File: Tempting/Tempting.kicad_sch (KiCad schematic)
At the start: 10 parts, among them U101 STM32WB55CGUx, U102 SCD41-D-R2

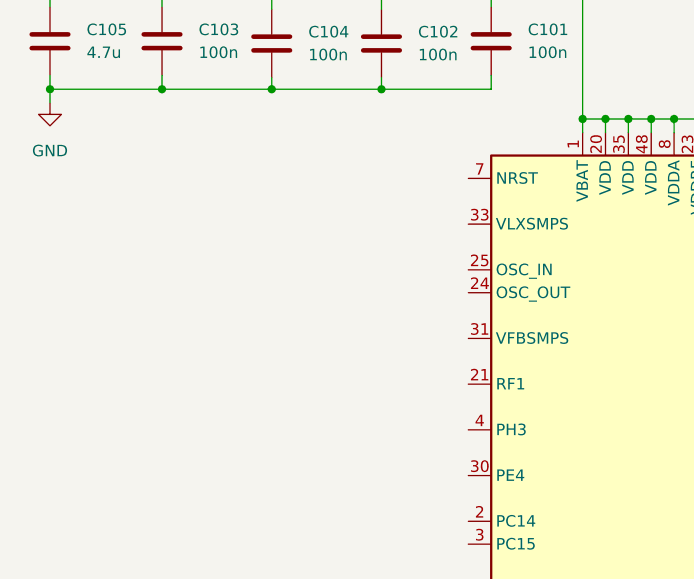
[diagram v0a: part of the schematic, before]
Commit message: Added crystals
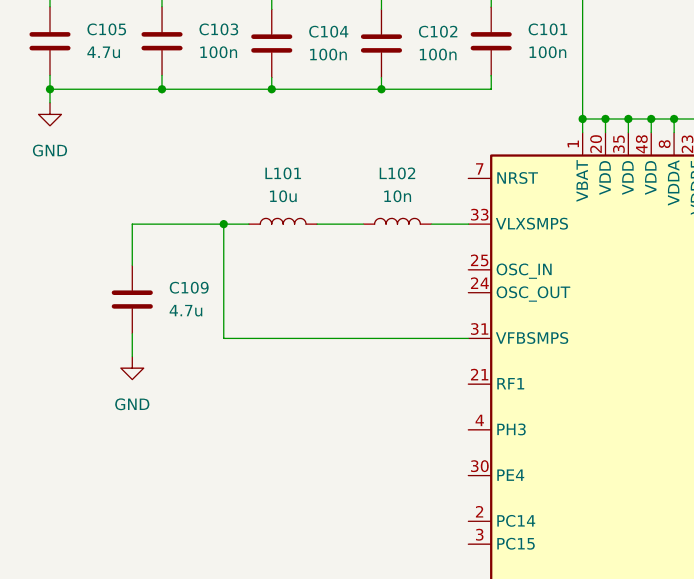
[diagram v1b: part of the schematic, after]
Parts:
- added C109: 4.7u, symbol Device:C
- added L101: 10u, symbol Device:L
- added L102: 10n, symbol Device:L
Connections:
- net GND: now also C109.2
- net at U101.31 (VFBSMPS): now also C109.1, L101.1
- net at U101.33 (VLXSMPS): now also L102.2
- new net: L101.2, L102.1

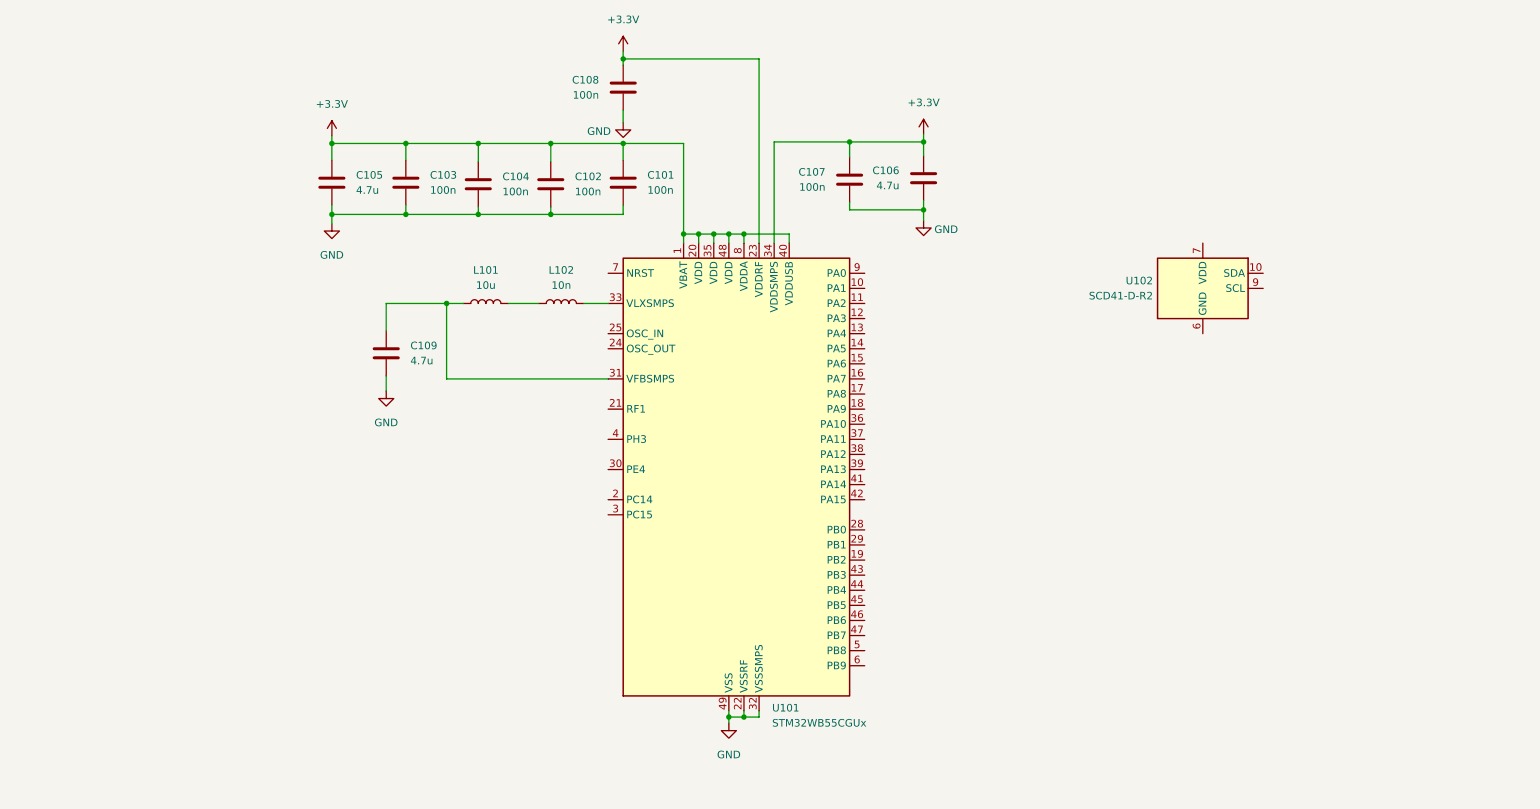
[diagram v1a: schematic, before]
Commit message: Added RF circuitry to schematic
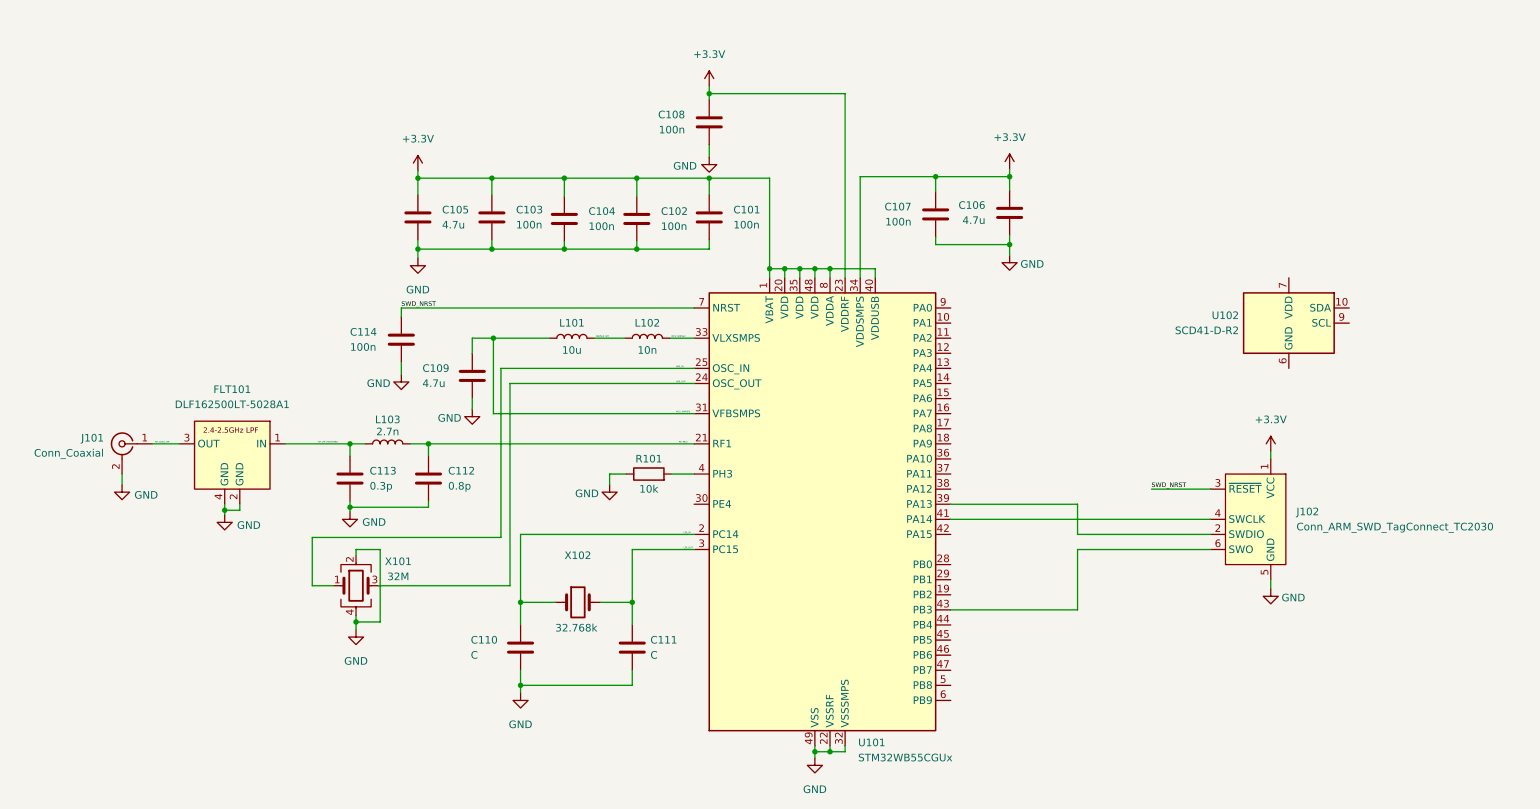
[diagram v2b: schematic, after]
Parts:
- added C110, C111: C, symbol Device:C
- added C112: 0.8p, symbol Device:C
- added C113: 0.3p, symbol Device:C
- added C114: 100n, symbol Device:C
- added FLT101: DLF162500LT-5028A1, Tempting_Footprint_Libraries:DLF162500LT-5028A1, symbol Tempting_Symbol_Libraries:DLF162500LT-5028A1
- added J101: Conn_Coaxial, symbol Connector:Conn_Coaxial
- added J102: Conn_ARM_SWD_TagConnect_TC2030, Connector:Tag-Connect_TC2030-IDC-FP_2x03_P1.27mm_Vertical, symbol Connector:Conn_ARM_SWD_TagConnect_TC2030
- added L103: 2.7n, symbol Device:L
- added R101: 10k, symbol Device:R
- added X101: 32M, symbol Device:Crystal_GND24
- added X102: 32.768k, symbol Device:Crystal
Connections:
- net +3.3V: now also J102.1 (VCC)
- net GND: now also C110.2, C111.2, C112.2, C113.2, C114.2, FLT101.2 (GND), FLT101.4 (GND), J101.2 (Ext), J102.5 (GND), R101.1, X101.2, X101.4
- net MCU_SMPSFB: now reaches C109.1, L101.1, U101.31 (VFBSMPS)
- net LSE_IN: now reaches U101.2 (PC14)
- net LSE_IN: now also C110.1, X102.1
- net RF_MCU: now reaches U101.21 (RF1)
- net RF_MCU: now also C112.1, L103.2
- net HSE_OUT: now reaches U101.24 (OSC_OUT)
- net HSE_OUT: now also X101.3
- net HSE_IN: now reaches U101.25 (OSC_IN)
- net HSE_IN: now also X101.1
- net LSE_OUT: now reaches U101.3 (PC15)
- net LSE_OUT: now also C111.1, X102.2
- net MCU_SMPSLX: now reaches L102.2, U101.33 (VLXSMPS)
- net at U101.39 (PA13): now also J102.2 (SWDIO)
- net at U101.4 (PH3): now also R101.2
- net at U101.41 (PA14): now also J102.4 (SWCLK)
- net at U101.43 (PB3): now also J102.6 (SWO)
- net SWD_NRST: now reaches U101.7 (NRST)
- net SWD_NRST: now also C114.1, J102.3 (~{RESET})
- net SMPSLX_INT: now reaches L101.2, L102.1
- new net RF_COAX_LPF: FLT101.3 (OUT), J101.1 (In)
- new net RF_LPF_MATCHING: C113.1, FLT101.1 (IN), L103.1
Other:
- moved on the sheet: C101, C102, C103, C104, C105, C106, C107, C108, C109, L101, L102, U101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

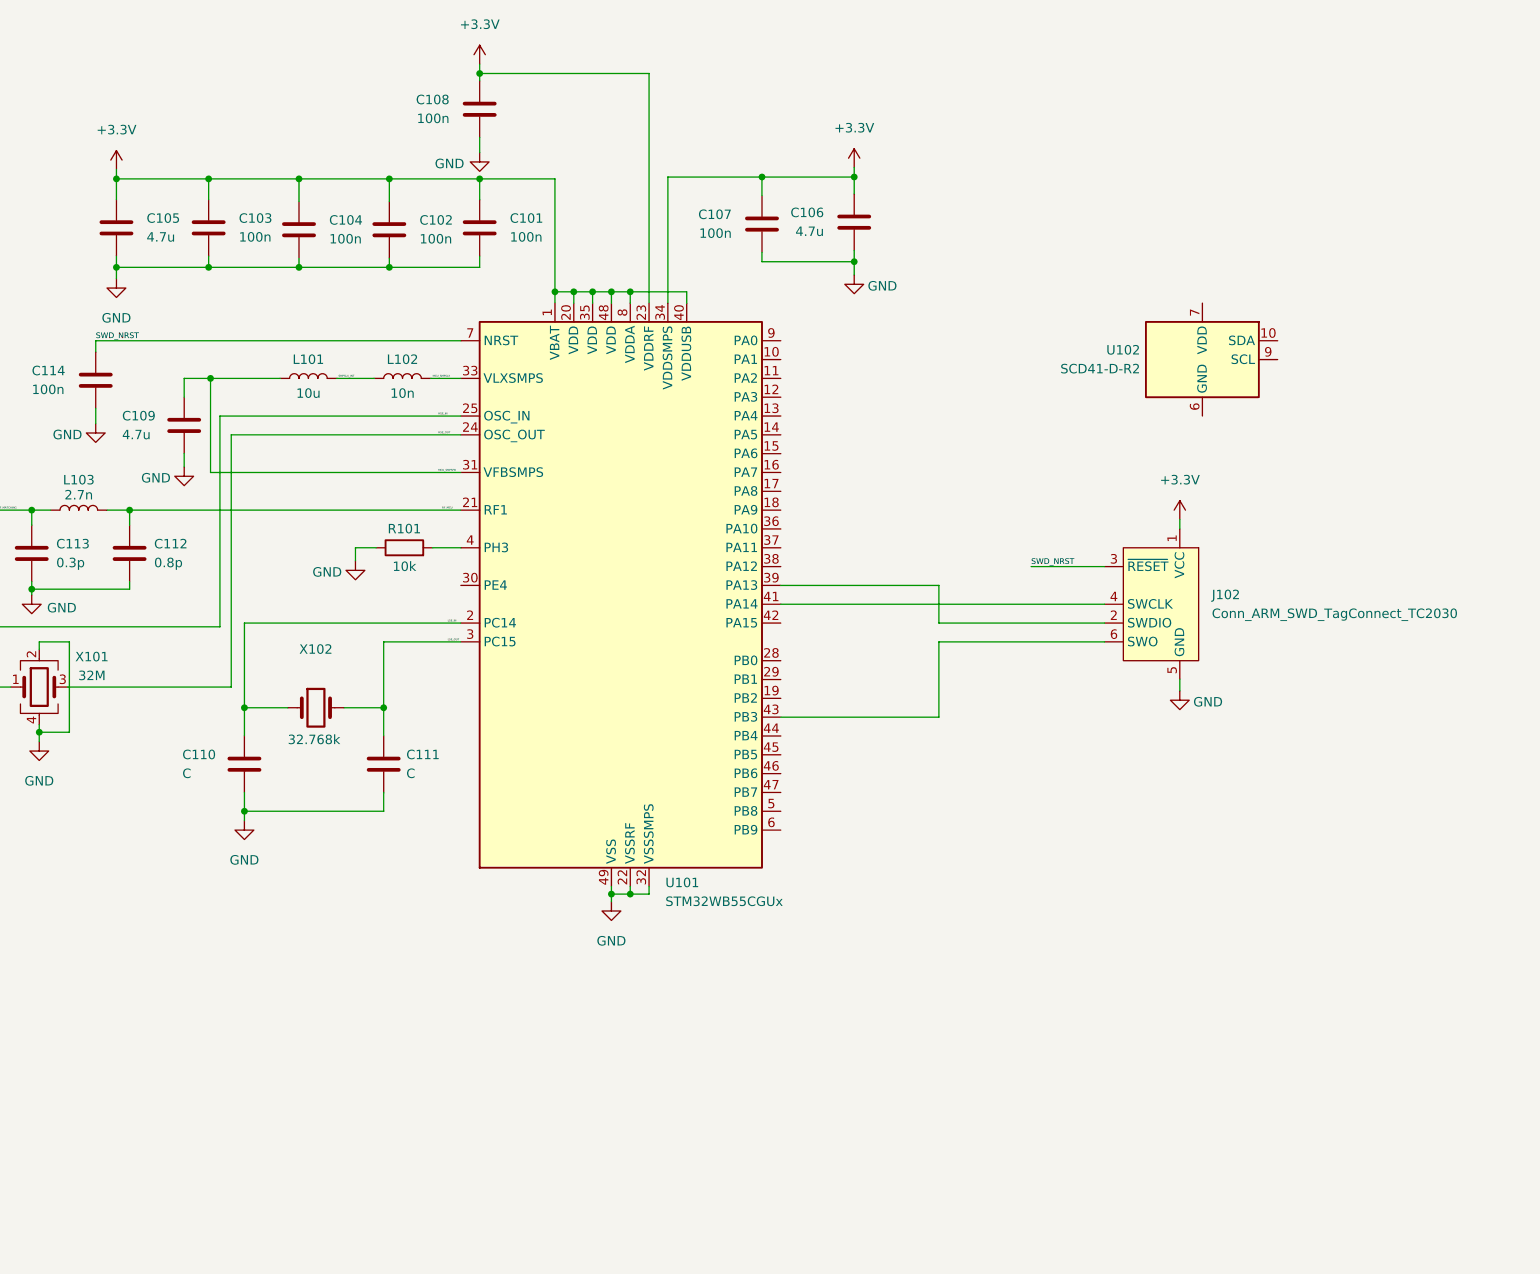
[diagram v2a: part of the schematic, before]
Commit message: Added USB connector
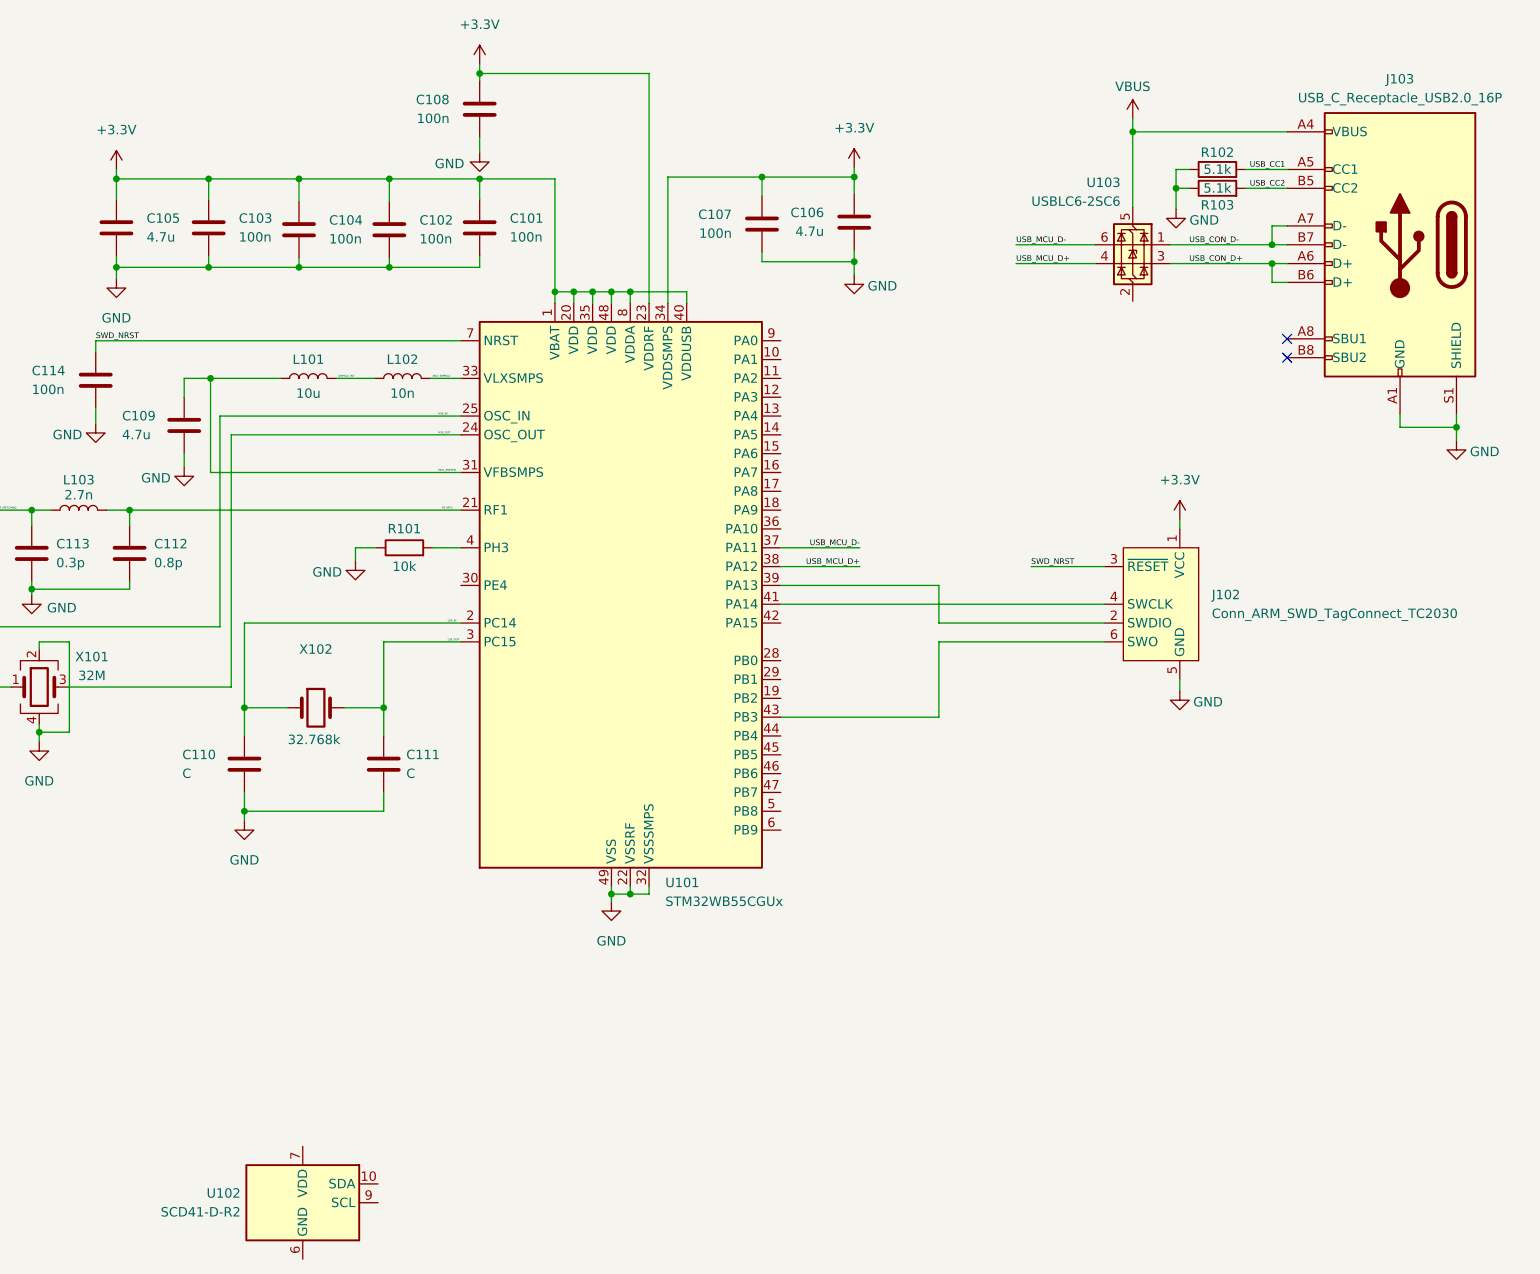
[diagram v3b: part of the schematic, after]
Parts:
- added J103: USB_C_Receptacle_USB2.0_16P, symbol Connector:USB_C_Receptacle_USB2.0_16P
- added R102, R103: 5.1k, symbol Device:R
- added U103: USBLC6-2SC6, Package_TO_SOT_SMD:SOT-23-6, symbol Power_Protection:USBLC6-2SC6
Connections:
- net GND: now also J103.A1 (GND), J103.A12 (GND), J103.B1 (GND), J103.B12 (GND), J103.S1 (SHIELD), R102.1, R103.1
- net USB_MCU_D-: now reaches U101.37 (PA11)
- net USB_MCU_D-: now also U103.6 (I/O1)
- net USB_MCU_D+: now reaches U101.38 (PA12)
- net USB_MCU_D+: now also U103.4 (I/O2)
- new net USB_CC1: J103.A5 (CC1), R102.2
- new net USB_CC2: J103.B5 (CC2), R103.2
- new net USB_CON_D+: J103.A6 (D+), J103.B6 (D+), U103.3 (I/O2)
- new net USB_CON_D-: J103.A7 (D-), J103.B7 (D-), U103.1 (I/O1)
- new net VBUS: J103.A4 (VBUS), J103.A9 (VBUS), J103.B4 (VBUS), J103.B9 (VBUS), U103.5 (VBUS)
- no-connect marks 0 -> 2
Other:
- moved on the sheet: U102

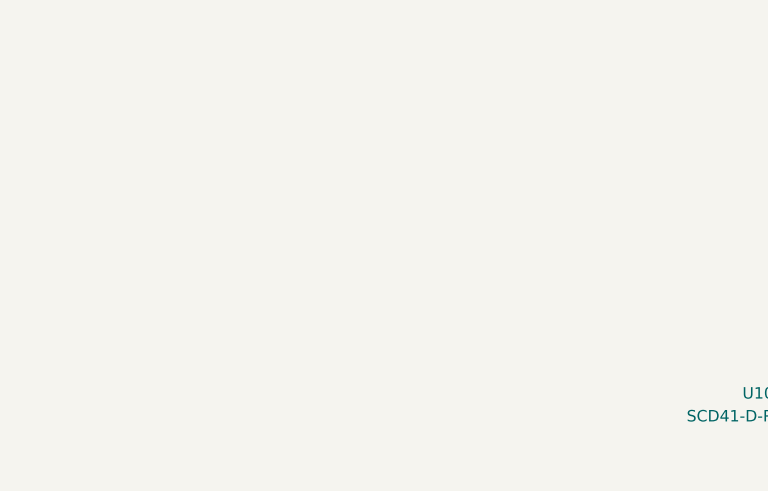
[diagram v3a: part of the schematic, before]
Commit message: Added LDO
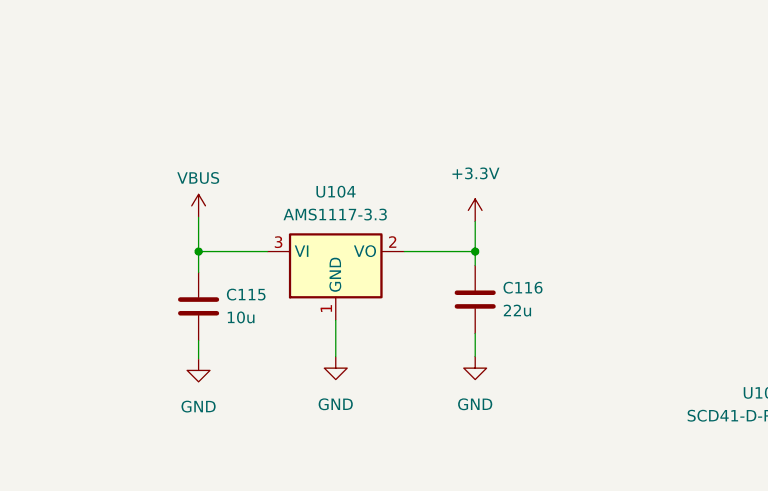
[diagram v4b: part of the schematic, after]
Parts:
- added C115: 10u, symbol Device:C
- added C116: 22u, symbol Device:C
- added U104: AMS1117-3.3, Package_TO_SOT_SMD:SOT-223-3_TabPin2, symbol Regulator_Linear:AMS1117-3.3
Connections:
- net +3.3V: now also C116.1, U104.2 (VO)
- net GND: now also C115.2, C116.2, U104.1 (GND)
- net VBUS: now also C115.1, U104.3 (VI)
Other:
- company: (none) -> Tempting Services
- title: (none) -> Tempting
